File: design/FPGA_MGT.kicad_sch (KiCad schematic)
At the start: 3 parts

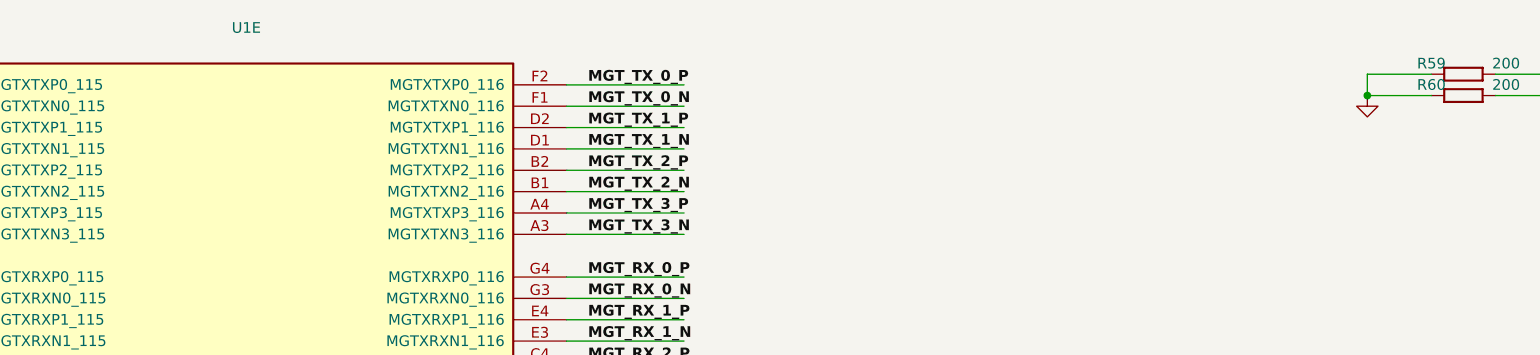
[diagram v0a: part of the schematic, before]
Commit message: new power converter added
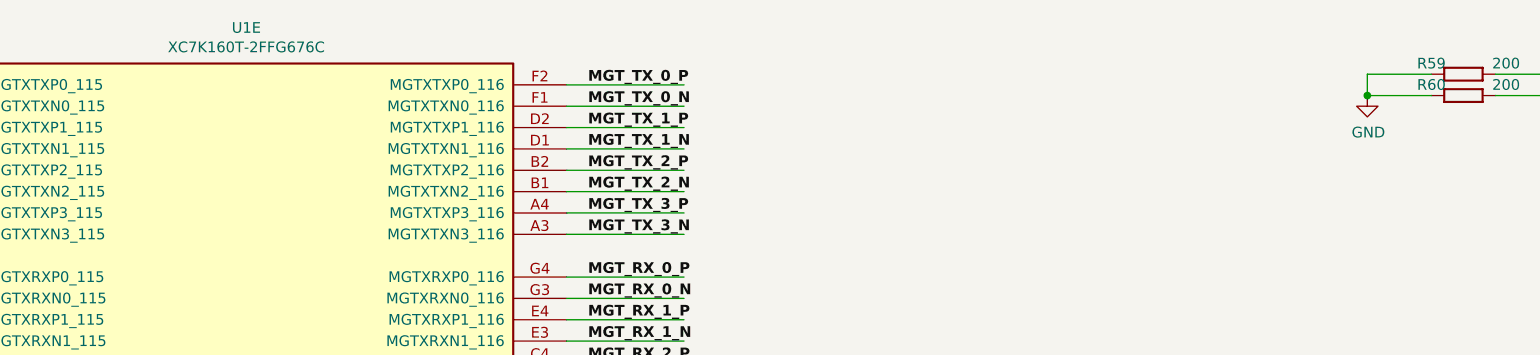
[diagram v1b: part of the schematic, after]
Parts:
- R59, R60: value (none) -> R0201_200R_1%_0.05W_200PPM; footprint (none) -> RESC0603X28N
- U1: value (none) -> XC7K160T-2FFG676C; footprint (none) -> ICs And Semiconductors SMD_BGA:BGA676C100P26X26_2700X2700X260
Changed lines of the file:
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@@
     (in_bom yes) (on_board yes)
     (property "Reference" "R59" (id 0) (at 210.82 19.05 0))
-    (property "Value" "" (id 1) (at 210.82 25.654 0)
-      (effects (font (size 1.524 1.524)) (justify left) hide)
-    )
-    (property "Footprint" "" (id 2) (at 210.82 46.228 0)
+    (property "Value" "R0201_200R_1%_0.05W_200PPM" (id 1) (at 210.82 25.654 0)
+      (effects (font (size 1.524 1.524)) (justify left) hide)
+    )
+    (property "Footprint" "RESC0603X28N" (id 2) (at 210.82 46.228 0)
       (effects (font (size 1.524 1.524)) (justify left) hide)
     )
@@
     (in_bom yes) (on_board yes)
     (property "Reference" "R60" (id 0) (at 210.82 21.59 0))
-    (property "Value" "" (id 1) (at 210.82 28.194 0)
-      (effects (font (size 1.524 1.524)) (justify left) hide)
-    )
-    (property "Footprint" "" (id 2) (at 210.82 48.768 0)
+    (property "Value" "R0201_200R_1%_0.05W_200PPM" (id 1) (at 210.82 28.194 0)
+      (effects (font (size 1.524 1.524)) (justify left) hide)
+    )
+    (property "Footprint" "RESC0603X28N" (id 2) (at 210.82 48.768 0)
       (effects (font (size 1.524 1.524)) (justify left) hide)
     )
@@
     (in_bom yes) (on_board yes)
     (property "Reference" "U1" (id 0) (at 69.85 14.8082 0))
-    (property "Value" "" (id 1) (at 69.85 17.1196 0))
-    (property "Footprint" "" (id 2) (at 69.85 49.53 0)
+    (property "Value" "XC7K160T-2FFG676C" (id 1) (at 69.85 17.1196 0))
+    (property "Footprint" "ICs And Semiconductors SMD_BGA:BGA676C100P26X26_2700X2700X260" (id 2) (at 69.85 49.53 0)
       (effects (font (size 1.27 1.27)) hide)
     )
@@
   (symbol (lib_id "power:GND") (at 203.2 22.86 0) (unit 1)
     (in_bom yes) (on_board yes)
-    (property "Reference" "#PWR?" (id 0) (at 203.2 29.21 0)
+    (property "Reference" "#PWR0493" (id 0) (at 203.2 29.21 0)
       (effects (font (size 1.27 1.27)) hide)
     )
-    (property "Value" "" (id 1) (at 203.327 27.2542 0))
+    (property "Value" "GND" (id 1) (at 203.327 27.2542 0))
     (property "Footprint" "" (id 2) (at 203.2 22.86 0)
       (effects (font (size 1.27 1.27)) hide)

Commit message: connected signals to the J9 connector
connected signals to the J9 connector
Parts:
- R59, R60: Author CERN DEM JLC -> (none)
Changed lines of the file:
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@@
       (effects (font (size 1.524 1.524)) (justify left) hide)
     )
-    (property "Author" "CERN DEM JLC" (id 36) (at 210.82 107.95 0)
+    (property "Author" "" (id 36) (at 210.82 107.95 0)
       (effects (font (size 1.524 1.524)) (justify left) hide)
     )
@@
       (effects (font (size 1.524 1.524)) (justify left) hide)
     )
-    (property "Author" "CERN DEM JLC" (id 36) (at 210.82 110.49 0)
+    (property "Author" "" (id 36) (at 210.82 110.49 0)
       (effects (font (size 1.524 1.524)) (justify left) hide)
     )
